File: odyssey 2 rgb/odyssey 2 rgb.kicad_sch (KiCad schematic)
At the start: 56 parts, among them J1 SCART-F, J10 c-sync? (pin 5, 8245), J11 c-sync out, J12 Composite video, J13 Composite video/sync to scart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, J14 5v, J15 12v, J16 GND, J2 SND (pin 27, 8245), J3 C. BLK (pin 39, 8048), J4 L (pin 10, 8245), J5 P17 (pin 34, 8048), J6 R (pin 18, 8245), J7 G (pin 19, 8245), J8 B (pin 20, 8245), J9 Comp. (pin 5, color encoder), Q1 BC548, Q2 BC548, Q3 BC558, Q4 BC548, U1 7407, U2 74LS08, U3 74LS00

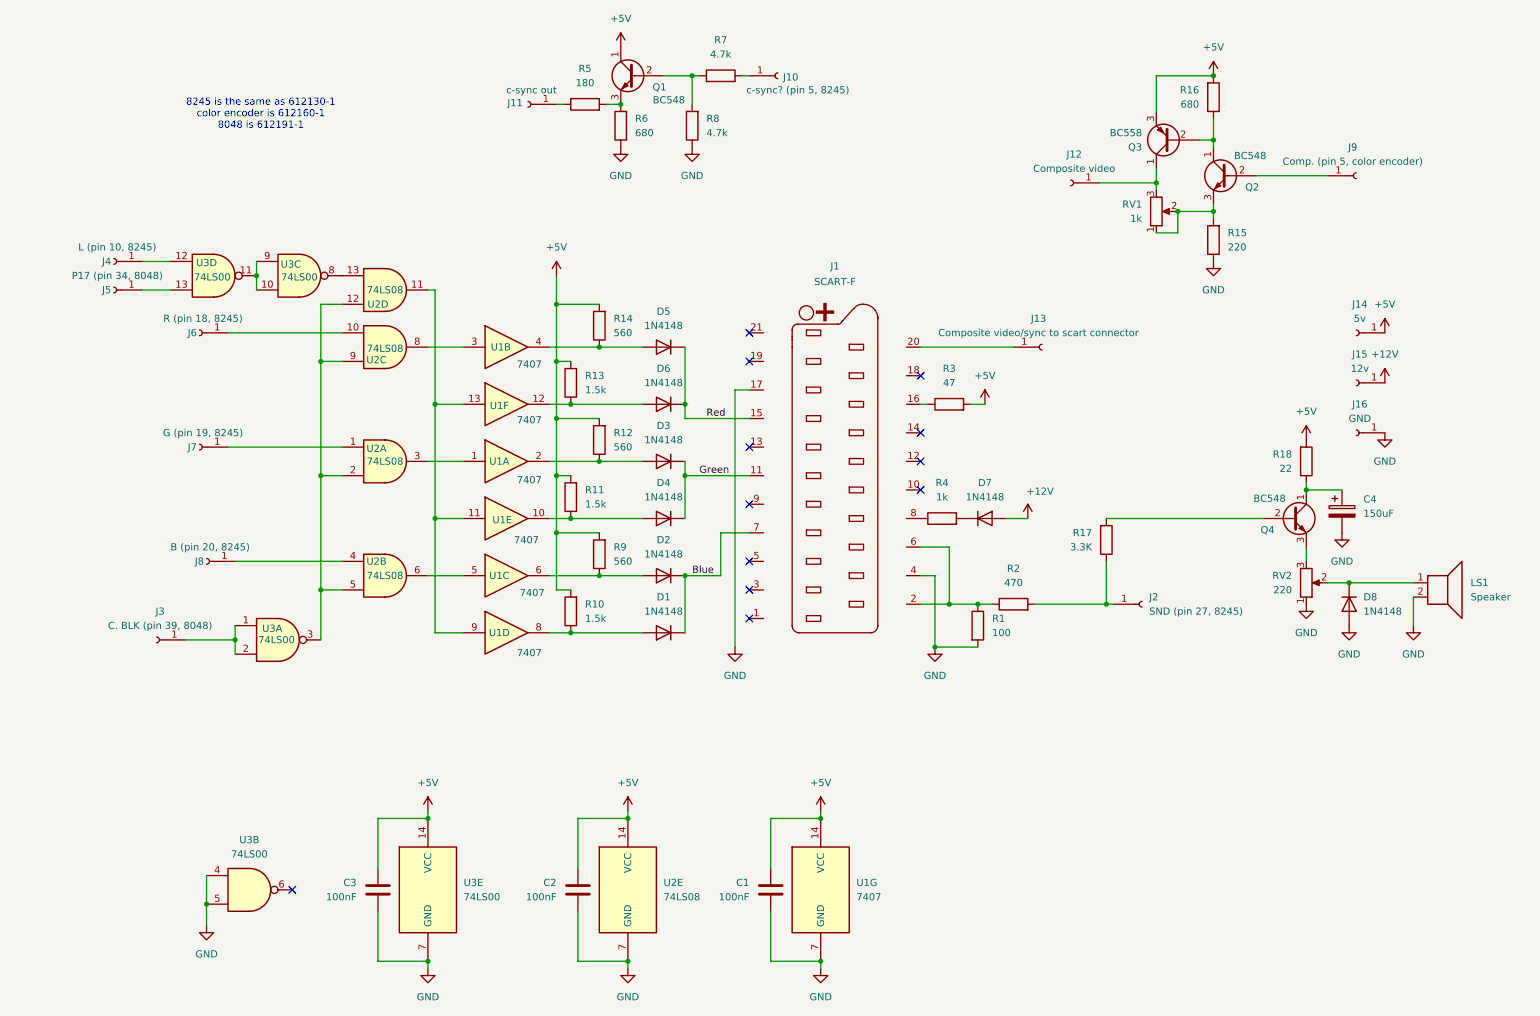
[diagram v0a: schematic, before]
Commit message: updating odyssey 2 rgb pcb
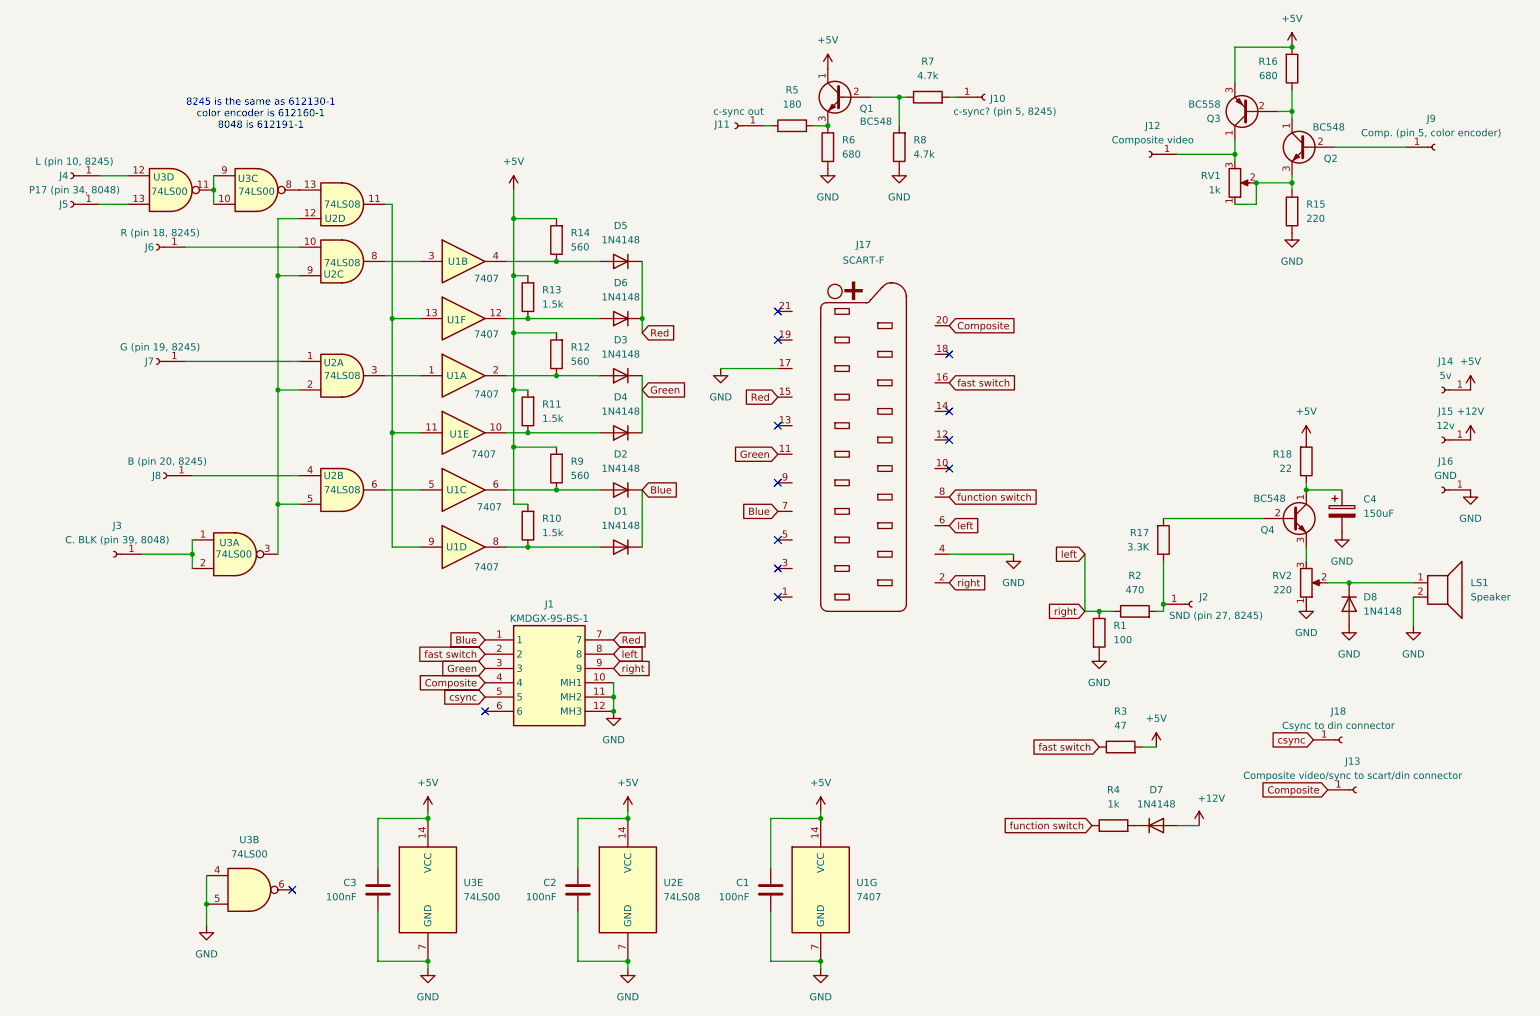
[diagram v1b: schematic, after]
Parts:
- removed J1: SCART-F, Evan's misc parts:SCART-F, symbol Connector:SCART-F
- added J1: KMDGX-9S-BS-1, Evan's parts:KMDGX9SBS1, symbol Evan's parts:KMDGX-9S-BS-1
- added J17: SCART-F, Evan's misc parts:SCART-F, symbol Connector:SCART-F
- added J18: Csync to din connector, Connector_PinSocket_2.54mm:PinSocket_1x01_P2.54mm_Vertical, symbol Connector:Conn_01x01_Socket
- C1, C2, C3: footprint (none) -> Capacitor_THT:C_Disc_D4.3mm_W1.9mm_P5.00mm
- J10, J11, J12, J14, J15, J16, J2, J3, J4, J5, J6, J7, J8, J9: footprint (none) -> Connector_PinSocket_2.54mm:PinSocket_1x01_P2.54mm_Vertical
- J13: value Composite video/sync to scart connector -> Composite video/sync to scart/din connector; footprint (none) -> Connector_PinSocket_2.54mm:PinSocket_1x01_P2.54mm_Vertical
- LS1: footprint (none) -> Connector_PinSocket_2.54mm:PinSocket_2x01_P2.54mm_Vertical
- R1, R10, R11, R12, R13, R14, R15, R16, R17, R18, R2, R3, R4, R5, R6, R7, R8, R9: footprint (none) -> Resistor_THT:R_Axial_DIN0207_L6.3mm_D2.5mm_P7.62mm_Horizontal
- U1, U2, U3: footprint (none) -> Package_DIP:DIP-14_W7.62mm_LongPads
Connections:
- net Blue: now also J1.1, J17.7 (P7)
- net GND: now also J1.10 (MH1), J1.11 (MH2), J1.12 (MH3), J17.17 (P17), J17.4 (P4)
- net Green: now also J1.3, J17.11 (P11)
- net Red: now also J1.7, J17.15 (P15)
- net left: now reaches R1.1, R2.1
- net left: now also J1.8, J1.9, J17.2 (P2), J17.6 (P6)
- net fast switch: now reaches R3.1
- net fast switch: now also J1.2, J17.16 (P16)
- net Composite: now reaches J13.1 (Pin_1)
- net Composite: now also J1.4, J17.20 (P20)
- net function switch: now reaches R4.1
- net function switch: now also J17.8 (P8)
- new net csync: J1.5, J18.1 (Pin_1)
- no-connect marks 12 -> 13
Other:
- moved on the sheet: D1, D2, D3, D4, D5, D6, D7, J10, J11, J12, J13, J14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
